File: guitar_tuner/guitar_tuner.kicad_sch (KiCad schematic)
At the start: 8 parts, among them SW1 Reset, SW2 Boot, U1 ESP32-S2-SOLO

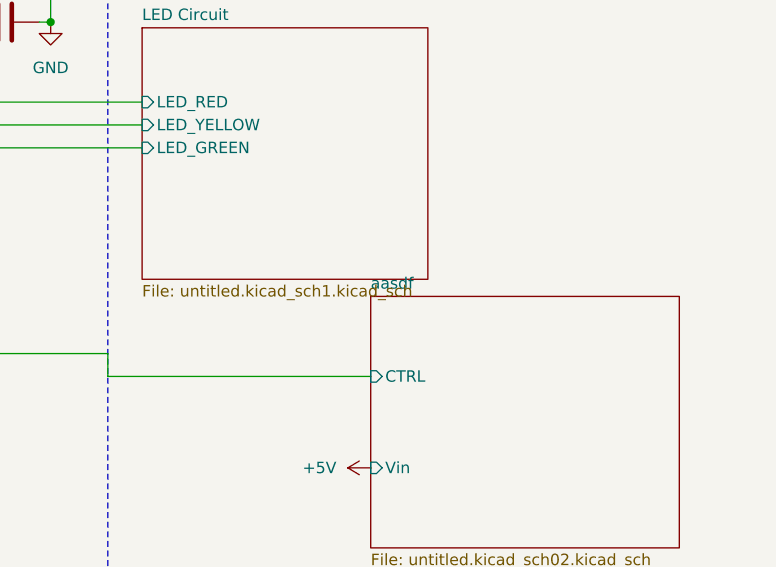
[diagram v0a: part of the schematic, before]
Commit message: Actual change to buzzer title
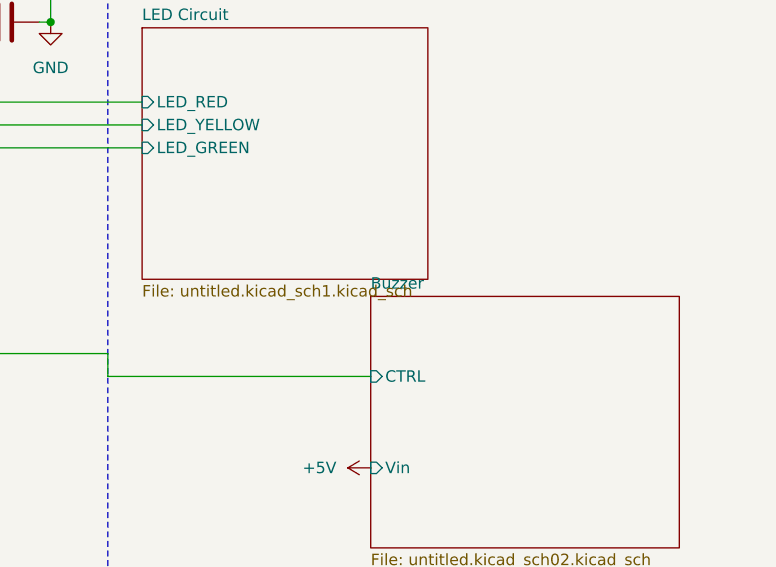
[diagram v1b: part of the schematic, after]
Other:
- sheet aasdf renamed Buzzer
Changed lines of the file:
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@@
 			(color 0 0 0 0.0000)
 		)
-		(property "Sheetname" "aasdf"
+		(property "Sheetname" "Buzzer"
 			(at 248.92 103.4284 0)
 			(effects

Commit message: Revert name change
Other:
- sheet Buzzer renamed aasdf
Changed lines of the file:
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@@
 			(color 0 0 0 0.0000)
 		)
-		(property "Sheetname" "Buzzer"
+		(property "Sheetname" "aasdf"
 			(at 248.92 103.4284 0)
 			(effects
